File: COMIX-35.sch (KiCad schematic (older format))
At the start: 18 parts, among them J1 Barrel_Jack_Switch, J2 EXPANSION, SW1 POWER, U3 74HC74, U4 74HC04, U5 74HC74, U6 74HC10, U7 74HC86, U8 74HC14

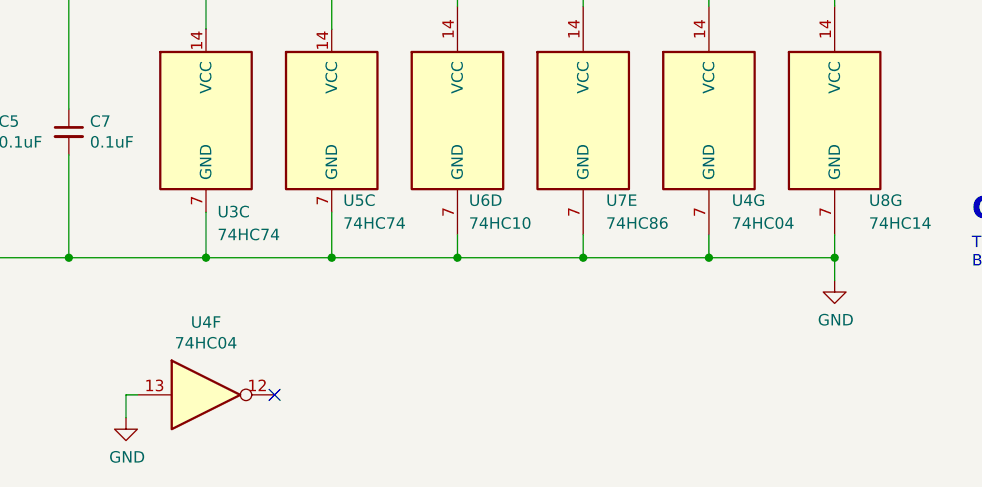
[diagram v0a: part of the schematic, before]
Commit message: U4 is now 74HCU04. Added comments in readme.
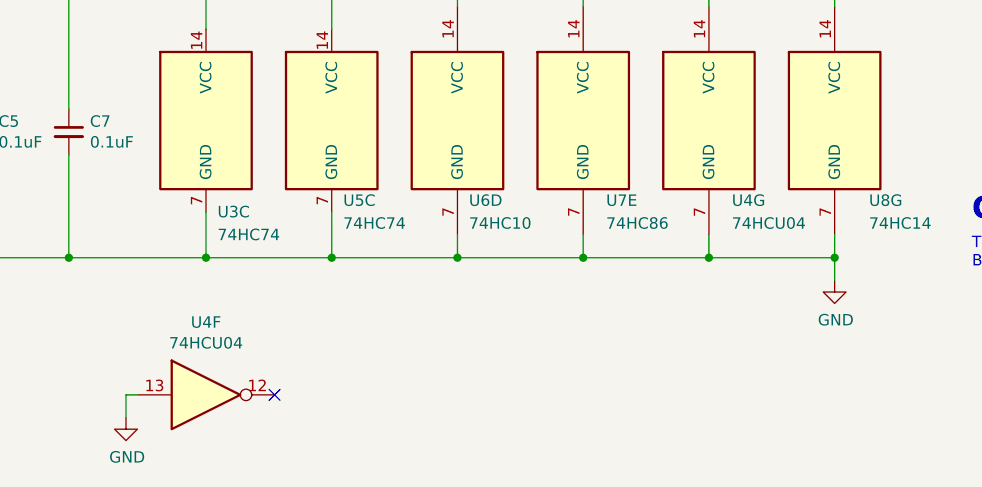
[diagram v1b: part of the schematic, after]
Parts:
- U4: value 74HC04 -> 74HCU04; Mouser 595-SN74HC04N -> 595-SN74HCU04N
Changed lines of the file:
@@
 P 3750 7500
 F 0 "U4" H 3750 7817 50  0000 C CNN
-F 1 "74HC04" H 3750 7726 50  0000 C CNN
+F 1 "74HCU04" H 3750 7726 50  0000 C CNN
 F 2 "Active:DIP254P762X635-14" H 3750 7500 50  0001 C CNN
 F 3 "http://www.ti.com/lit/gpn/sn74LS04" H 3750 7500 50  0001 C CNN
-F 4 "595-SN74HC04N" H 0   0   50  0001 C CNN "Mouser"
+F 4 "595-SN74HCU04N" H 0   0   50  0001 C CNN "Mouser"
 	6    3750 7500
 	1    0    0    -1
@@
 P 5950 6300
 F 0 "U4" H 6050 5950 50  0000 L CNN
-F 1 "74HC04" H 6050 5850 50  0000 L CNN
+F 1 "74HCU04" H 6050 5850 50  0000 L CNN
 F 2 "Active:DIP254P762X635-14" H 5950 6300 50  0001 C CNN
 F 3 "http://www.ti.com/lit/gpn/sn74LS04" H 5950 6300 50  0001 C CNN
-F 4 "595-SN74HC04N" H 0   0   50  0001 C CNN "Mouser"
+F 4 "595-SN74HCU04N" H 0   0   50  0001 C CNN "Mouser"
 	7    5950 6300
 	1    0    0    -1
@@
 Wire Wire Line
 	3350 1300 3350 1400
-Wire Bus Line
-	1200 3450 1200 4150
-Wire Bus Line
-	3550 3350 3550 4150
-Wire Bus Line
-	3650 2050 3650 4250
-Wire Bus Line
-	1000 2050 1000 4250
 Text Notes 9100 7100 0    50   ~ 0
 This work is licensed under the Creative Commons\nAttribution-ShareAlike 4.0 International License.\nTo view a copy of this license, visit \nhttp://creativecommons.org/licenses/by-sa/4.0/\nor send a letter to Creative Commons, PO Box 1866,\nMountain View, CA 94042, USA.
@@
 Text Notes 7100 6950 0    50   ~ 0
 Top Level\nBy @TubeTimeUS
+Wire Bus Line
+	1200 3450 1200 4150
+Wire Bus Line
+	3550 3350 3550 4150
+Wire Bus Line
+	3650 2050 3650 4250
+Wire Bus Line
+	1000 2050 1000 4250
 $EndSCHEMATC
